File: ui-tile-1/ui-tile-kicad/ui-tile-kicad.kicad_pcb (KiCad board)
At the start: 2 copper layers, 26 parts, among them SW1 SKRPABE010, SW2 SKRPABE010, U1 RP2040, U2 W25Q16JVUXIQ, X1 12MHz

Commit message: continuing with ui-tile
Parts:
- U2: moved to B.Cu
- moved C12 59.4 mm to (137.8, 41.5), turned to -90 degrees
- moved C11 54.1 mm to (131.8, 41.2), turned to -90 degrees
- moved C16 53.9 mm to (139.2, 45.8), turned to 180 degrees
- moved C14 53.9 mm to (139.2, 41.5), turned to -90 degrees
- moved C17 52.6 mm to (138.8, 49.2), turned to 180 degrees
- moved C15 51.4 mm to (133.0, 41.2), turned to -90 degrees
- moved C21 51.1 mm to (126.5, 37.5)
- moved R3 51.0 mm to (135.5, 41.2), turned to -90 degrees
- moved C13 49.8 mm to (134.5, 54.0), turned to 90 degrees
- moved R2 48.6 mm to (134.2, 41.2), turned to -90 degrees
- moved U2 48.1 mm to (128.5, 42.5), turned to 90 degrees
- moved C18 47.0 mm to (133.5, 54.0), turned to 90 degrees
- moved C20 42.7 mm to (127.5, 45.8)
- moved C19 38.1 mm to (127.3, 49.2)
- moved U1 33.2 mm to (133.5, 48.2)
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
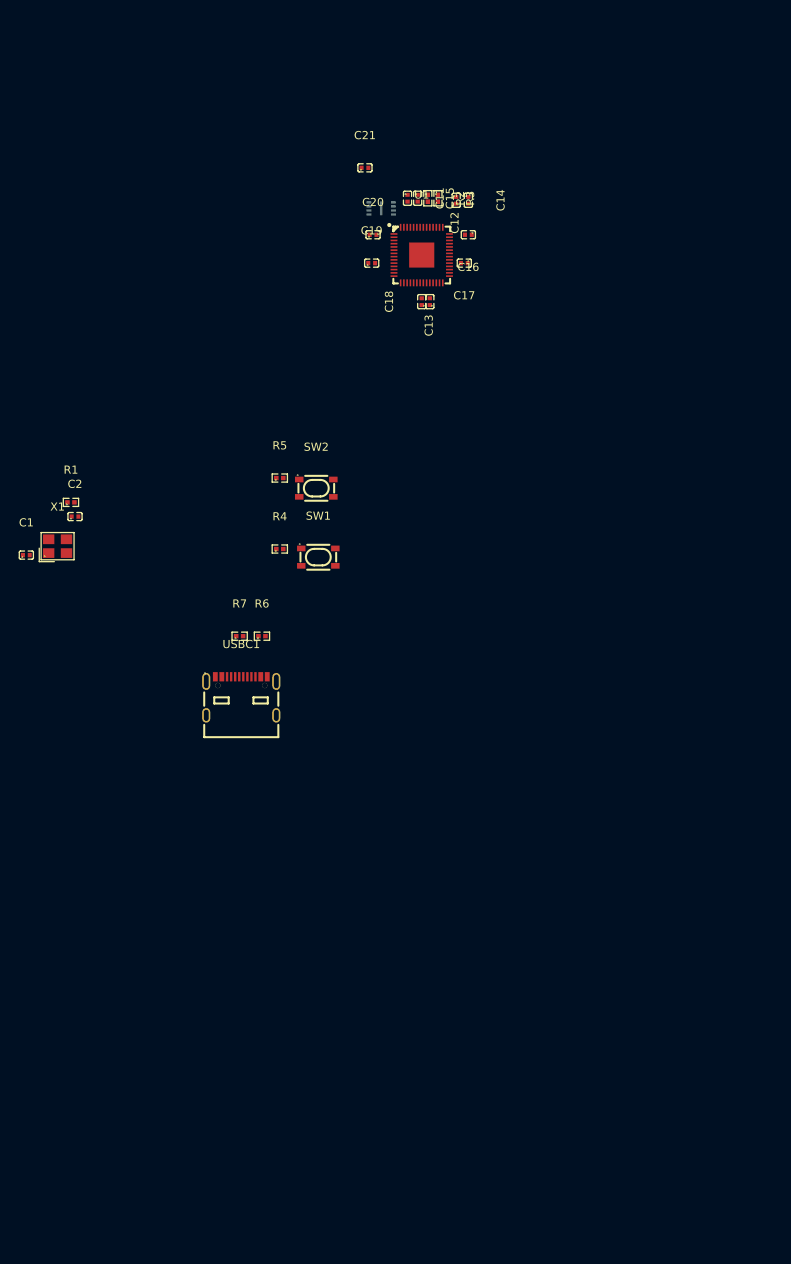
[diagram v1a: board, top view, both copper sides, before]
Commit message: removed warnings from schematic
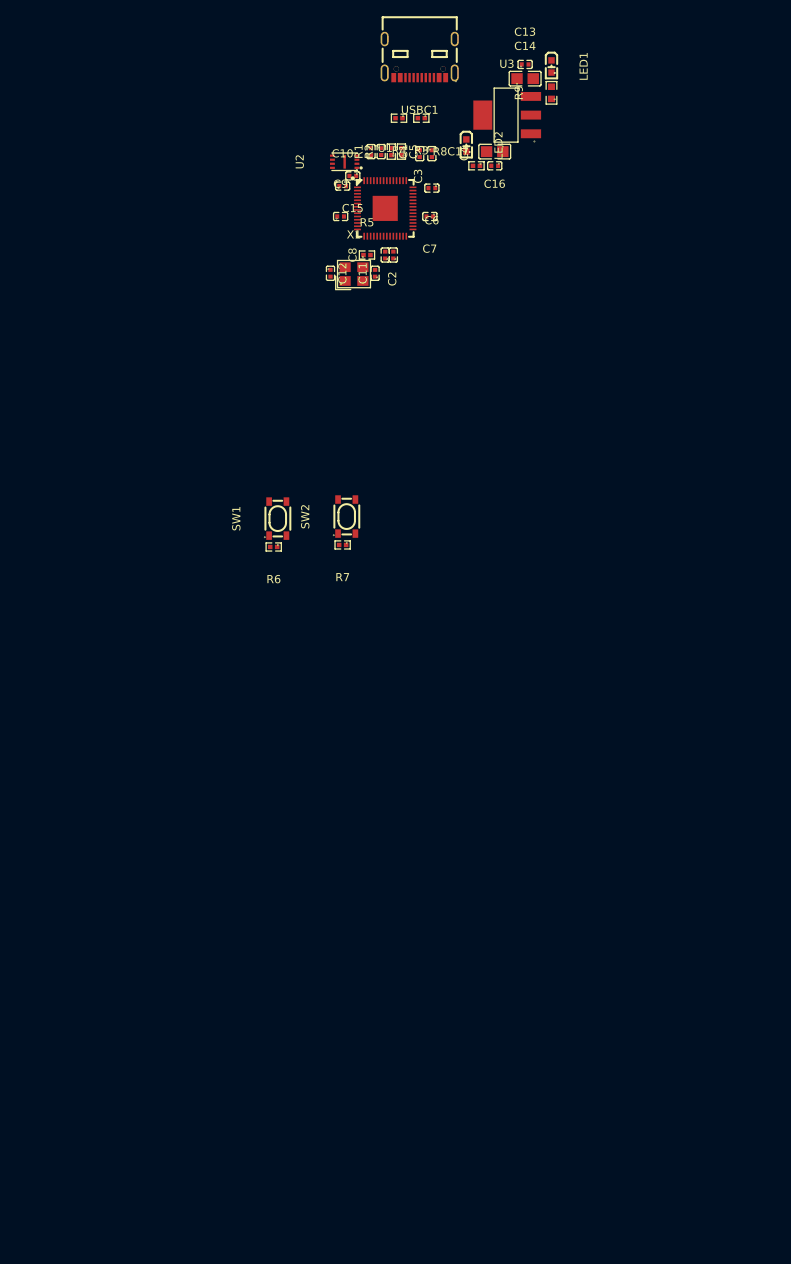
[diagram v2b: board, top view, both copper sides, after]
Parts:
- removed the C1 at (84.8, 85.2)
- removed the C2 at (90.8, 80.5)
- added C11: 30pF, jlcpcb:C0402, F.Cu at (122.2, 50.5)
- added C12: 30pF, jlcpcb:C0402, F.Cu at (127.8, 50.5)
- added C13: 100nF, jlcpcb:C0402, F.Cu at (146.2, 24.8)
- added C14: 10uF, jlcpcb:C0805, F.Cu at (146.2, 26.5)
- added C16: 10uF, jlcpcb:C0805, F.Cu at (142.5, 35.5)
- added C17: 100nF, jlcpcb:C0402, F.Cu at (142.5, 37.2)
- added LED1: KT-0603R, jlcpcb:LED-SMD_L1.6-W0.8-R-RD, F.Cu at (149.5, 25.0)
- added LED2: KT-0603R, jlcpcb:LED-SMD_L1.6-W0.8-R-RD, F.Cu at (139.0, 34.8)
- added R8: 1k, jlcpcb:R0402, F.Cu at (140.2, 37.2)
- added R9: 1.5k, jlcpcb:R0603, F.Cu at (149.5, 28.2)
- added U3: NCP1117ST33T3G, jlcpcb:SOT-223-3_L6.5-W3.4-P2.30-LS7.0-BR, F.Cu at (144.0, 31.0)
- U2: moved to F.Cu
- moved USBC1 81.6 mm to (133.2, 24.0), turned to 180 degrees
- moved R3 67.7 mm to (133.4, 31.4), turned to 180 degrees
- moved R4 66.1 mm to (130.7, 31.4), turned to 180 degrees
- moved X1 49.6 mm to (125.2, 50.6)
- moved R5 47.6 mm to (126.8, 48.2)
- moved R6 8.53 mm to (115.2, 84.2), turned to 180 degrees
- moved R7 7.77 mm to (123.8, 84.0), turned to 180 degrees
- moved C1 7.30 mm to (127.2, 35.5)
- moved C2 7.30 mm to (130.0, 48.2)
- moved C3 7.30 mm to (133.2, 35.8)
- moved C4 7.30 mm to (134.8, 35.8)
- moved C5 7.30 mm to (128.5, 35.5)
- moved C6 7.30 mm to (134.8, 40.0)
- moved C8 7.30 mm to (129.0, 48.2)
- moved R1 7.30 mm to (129.8, 35.5), turned to 90 degrees
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- renumbered C11 to C1, C20 to C10, C21 to C15, C13 to C2, C12 to C3, C14 to C4, C15 to C5, C16 to C6, C17 to C7, C18 to C8, C19 to C9, R2 to R1, R3 to R2, R7 to R3, R6 to R4, R1 to R5, R5 to R6, R4 to R7, SW2 to SW1, SW1 to SW2
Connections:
- R1 pad 1: Net-(U1-USB_DP) -> /USB_D+
- R1 pad 2: /USB_D+ -> Net-(U1-USB_DP)
- R2 pad 1: Net-(U1-USB_DM) -> /USB_D-
- R2 pad 2: /USB_D- -> Net-(U1-USB_DM)
- U1 pad 44: unconnected-(U1-VREG_IN-Pad44) -> +3V3
- U1 pad 52: /QSPI_CLK -> /QSPI_SCLK
- U2 pad 6: /QSP_SCLK -> /QSPI_SCLK

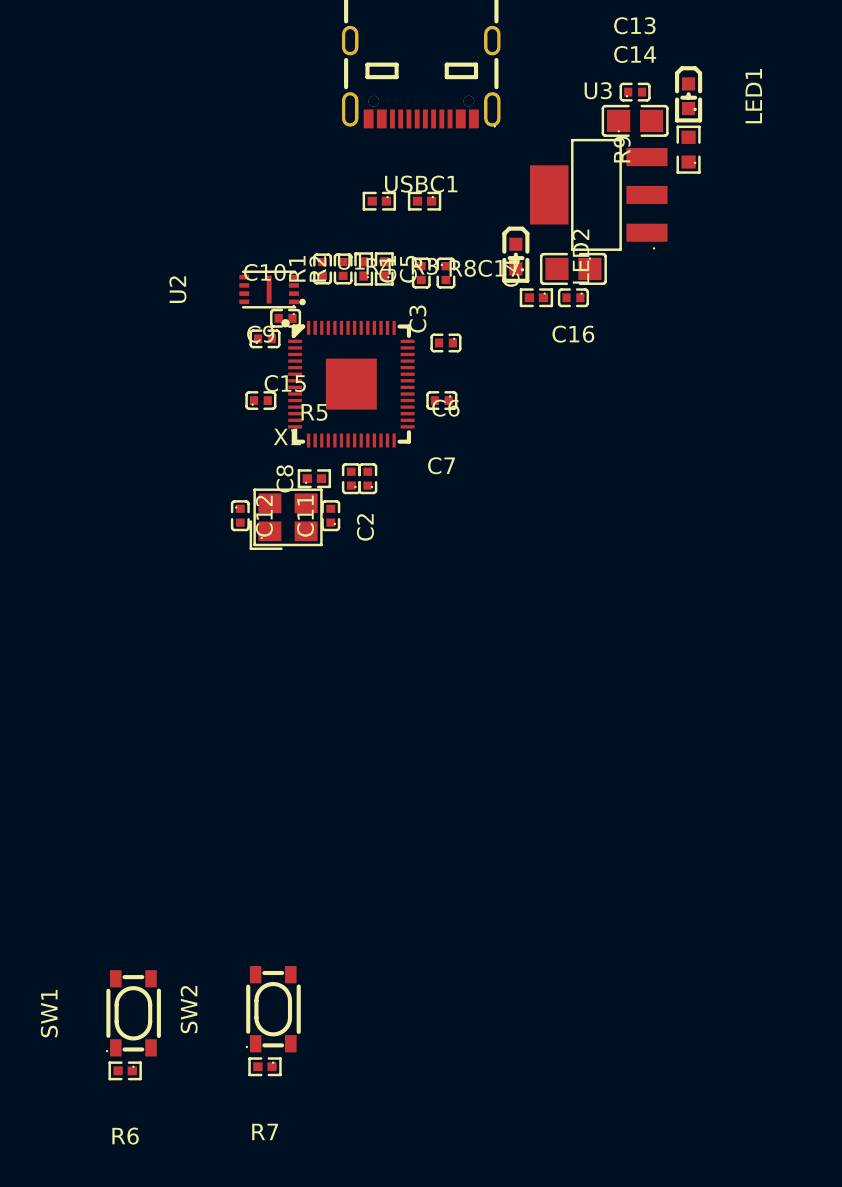
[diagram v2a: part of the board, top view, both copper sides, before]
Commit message: finished first pass at rp2040 basics
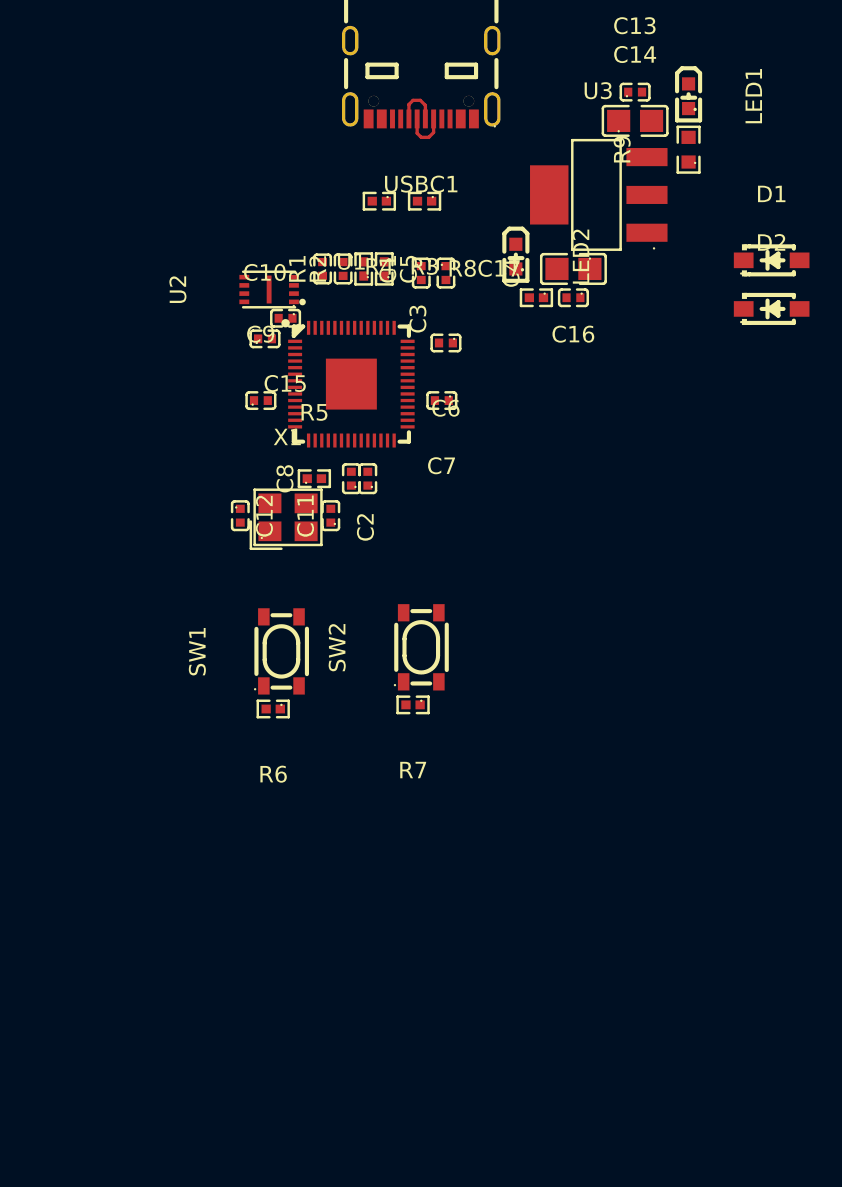
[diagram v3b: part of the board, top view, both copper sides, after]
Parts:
- added D1: B5819W_C8598, jlcpcb:SOD-123_L2.7-W1.6-LS3.7-RD-1, F.Cu at (154.6, 35.0)
- added D2: B5819W_C8598, jlcpcb:SOD-123_L2.7-W1.6-LS3.7-RD-1, F.Cu at (154.6, 37.9)
- moved R6 23.8 mm to (124.2, 62.2)
- moved R7 23.8 mm to (132.8, 62.0)
- moved SW1 23.8 mm to (124.8, 58.8)
- moved SW2 23.8 mm to (133.2, 58.5)
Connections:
- C13 pad 2: /USB_VSYS -> /VSYS
- C14 pad 2: /USB_VSYS -> /VSYS
- R9 pad 1: /USB_VSYS -> /VSYS
- U3 pad 3: /USB_VSYS -> /VSYS
- USBC1 pad A4-B9: /USB_VSYS -> /USB_VBUS
- USBC1 pad B4-A9: /USB_VSYS -> /USB_VBUS
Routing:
- net /USB_D+: track 0.00 -> 2.93 mm
- net /USB_D-: track 0.00 -> 2.92 mm

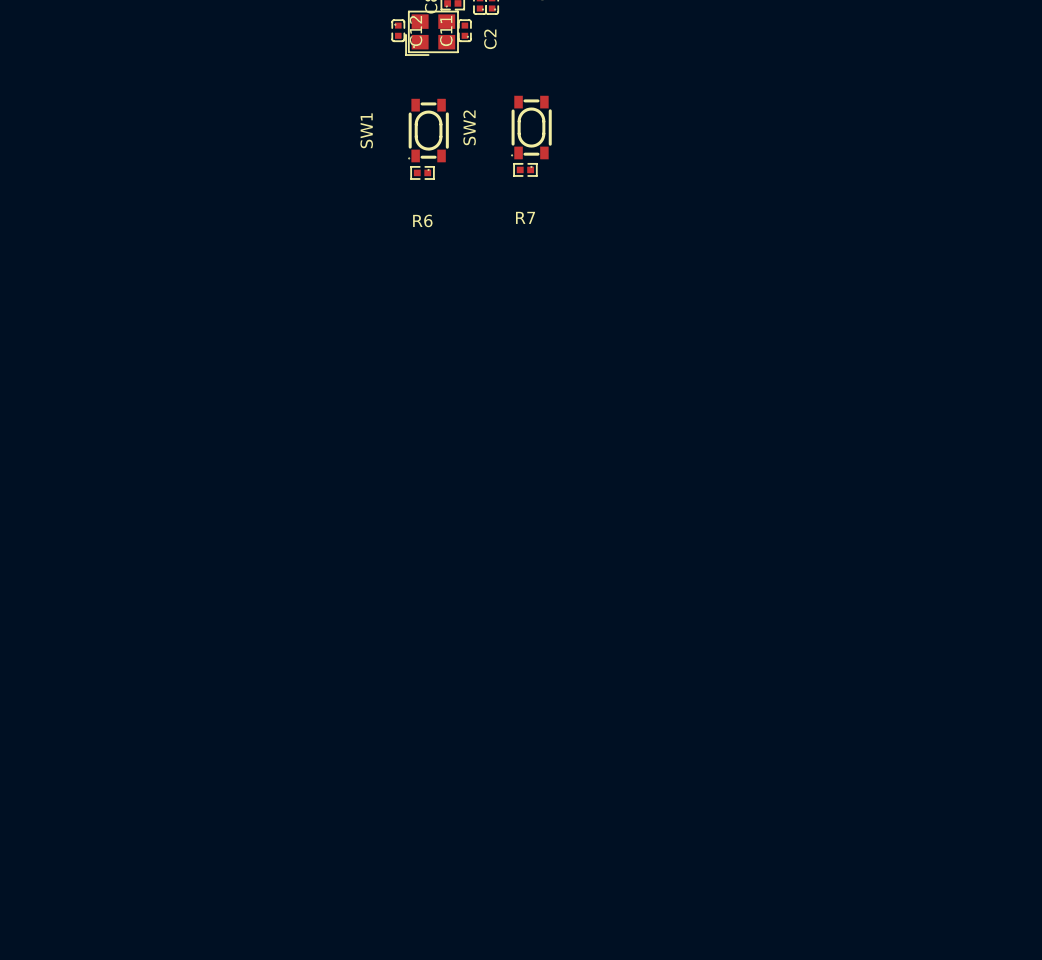
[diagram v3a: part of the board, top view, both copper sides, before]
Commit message: started breaking out into sub sheets
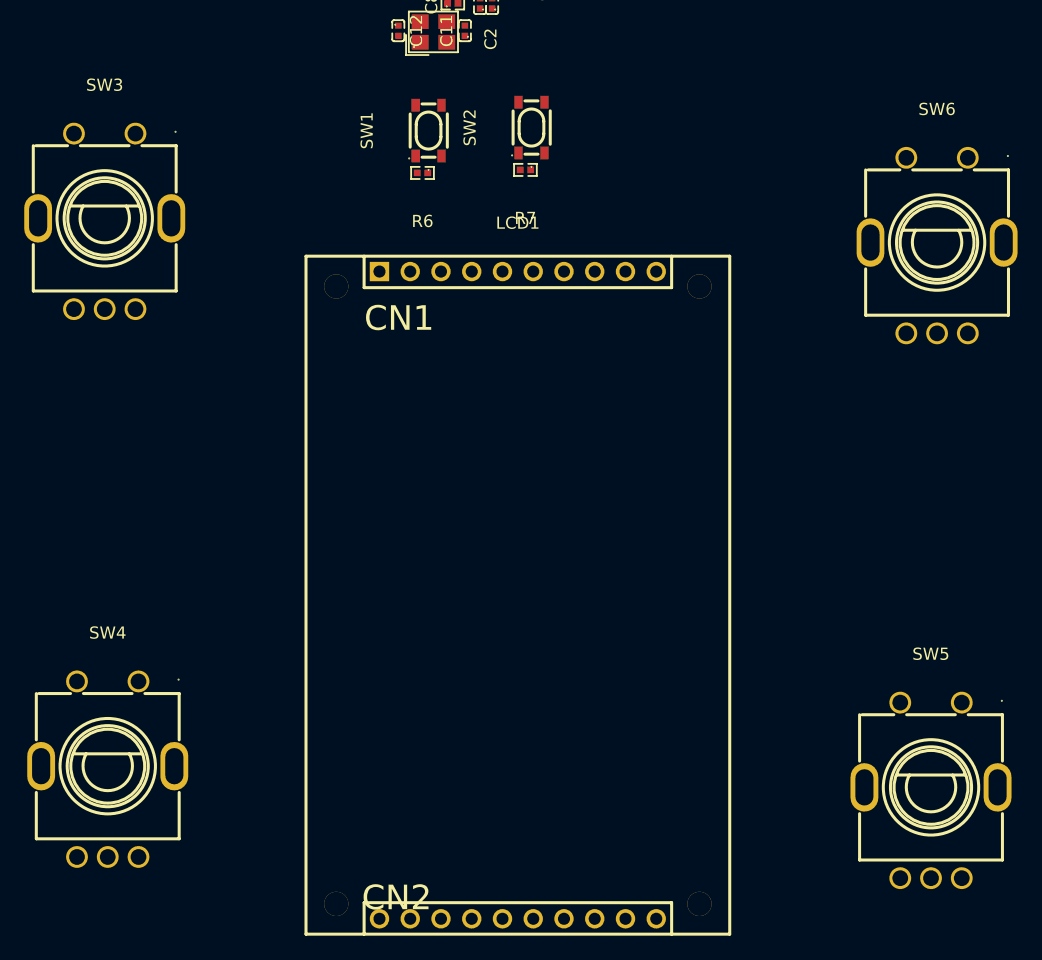
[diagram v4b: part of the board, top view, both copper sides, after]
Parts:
- added LCD1: HS180S10B, jlcpcb:LCD-TH_L56.0-W35.0-P2.54_HS180S10B, F.Cu at (132.1, 97.1)
- added SW3: EC11E15244G1, jlcpcb:SW-TH_EC11E15244G1, F.Cu at (98.0, 66.2)
- added SW4: EC11E15244G1, jlcpcb:SW-TH_EC11E15244G1, F.Cu at (98.2, 111.5)
- added SW5: EC11E15244G1, jlcpcb:SW-TH_EC11E15244G1, F.Cu at (166.2, 113.2)
- added SW6: EC11E15244G1, jlcpcb:SW-TH_EC11E15244G1, F.Cu at (166.8, 68.2)
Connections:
- net /+5V renamed /rp2040/+5V
- net /QSPI_SCLK renamed /rp2040/QSPI_SCLK
- net /QSPI_SD0 renamed /rp2040/QSPI_SD0
- net /QSPI_SD1 renamed /rp2040/QSPI_SD1
- net /QSPI_SD2 renamed /rp2040/QSPI_SD2
- net /QSPI_SD3 renamed /rp2040/QSPI_SD3
- net /QSPI_SS renamed /rp2040/QSPI_SS
- net /RUN renamed /rp2040/RUN
- net /USB_D+ renamed /rp2040/USB_D+
- net /USB_D- renamed /rp2040/USB_D-
- net /USB_VBUS renamed /rp2040/USB_VBUS
- net /VSYS renamed /rp2040/VSYS
- net /XIN renamed /rp2040/XIN
- net /XOUT renamed /rp2040/XOUT

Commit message: started on ws2812's
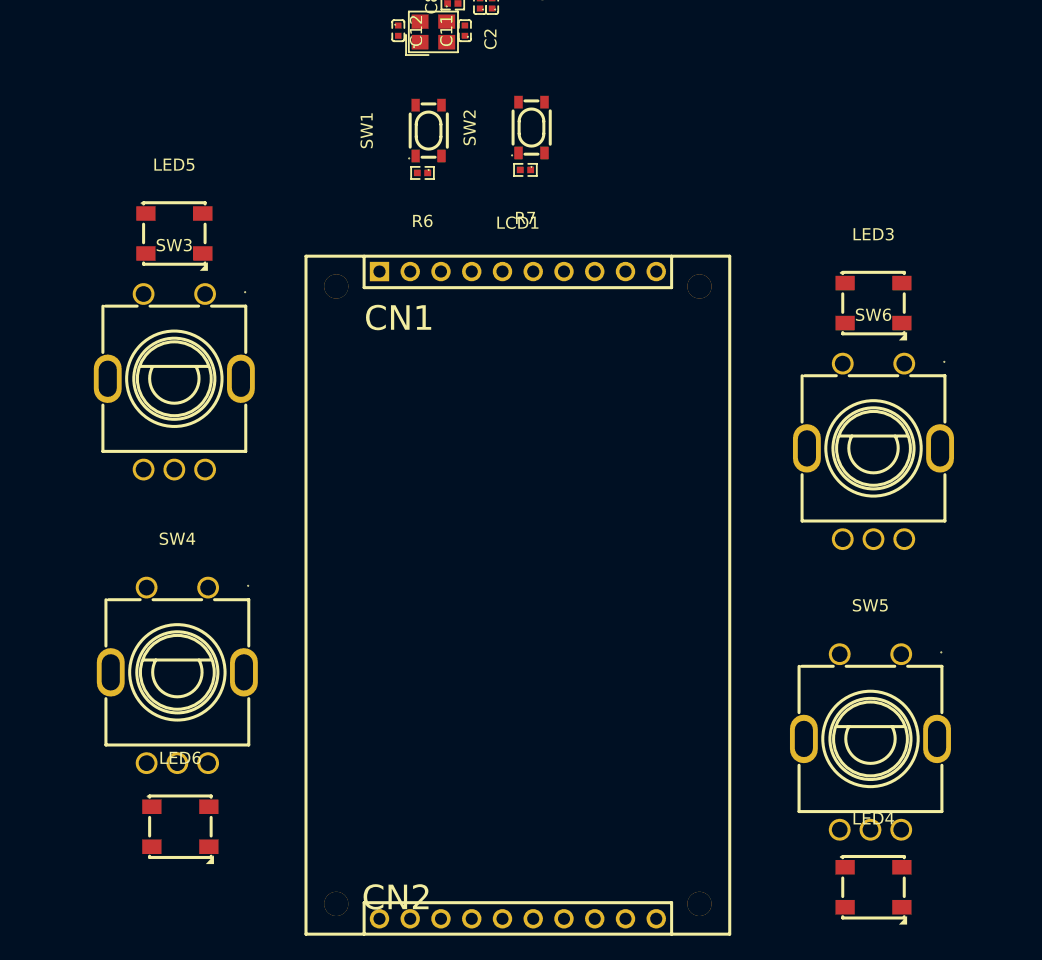
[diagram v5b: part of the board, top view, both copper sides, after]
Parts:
- added LED3: WS2812C, jlcpcb:LED-SMD_4P-L5.0-W5.0-LS5.4-TL-1, F.Cu at (161.5, 73.0)
- added LED4: WS2812C, jlcpcb:LED-SMD_4P-L5.0-W5.0-LS5.4-TL-1, F.Cu at (161.5, 121.2)
- added LED5: WS2812C, jlcpcb:LED-SMD_4P-L5.0-W5.0-LS5.4-TL-1, F.Cu at (103.8, 67.2)
- added LED6: WS2812C, jlcpcb:LED-SMD_4P-L5.0-W5.0-LS5.4-TL-1, F.Cu at (104.2, 116.2)
- moved SW6 17.8 mm to (161.5, 85.2)
- moved SW3 14.4 mm to (103.8, 79.5)
- moved SW4 9.65 mm to (104.0, 103.8)
- moved SW5 6.40 mm to (161.2, 109.2)
